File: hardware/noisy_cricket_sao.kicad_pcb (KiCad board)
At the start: 2 copper layers, 30 x 25 mm, 26 parts, among them J1 SAO 6-Pin, U1 AD8107, U2 CH32V003F4U6

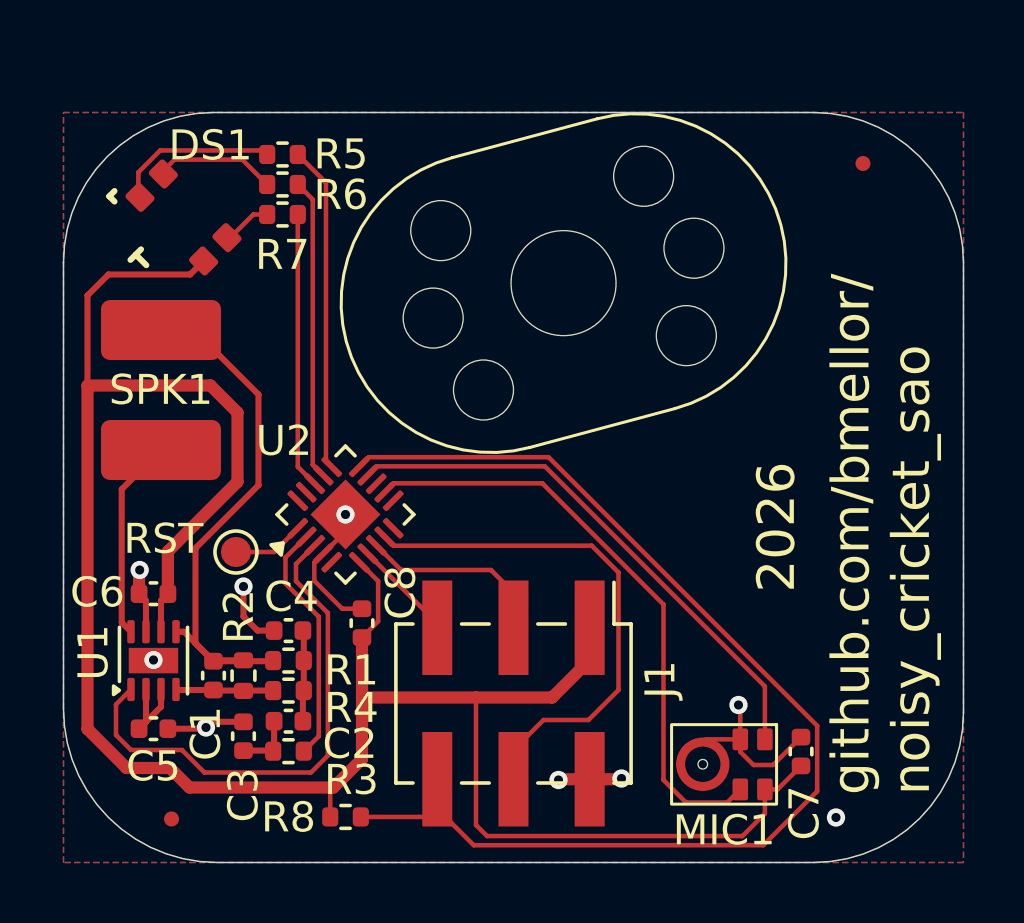
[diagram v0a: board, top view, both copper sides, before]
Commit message: Switch to MSPM0
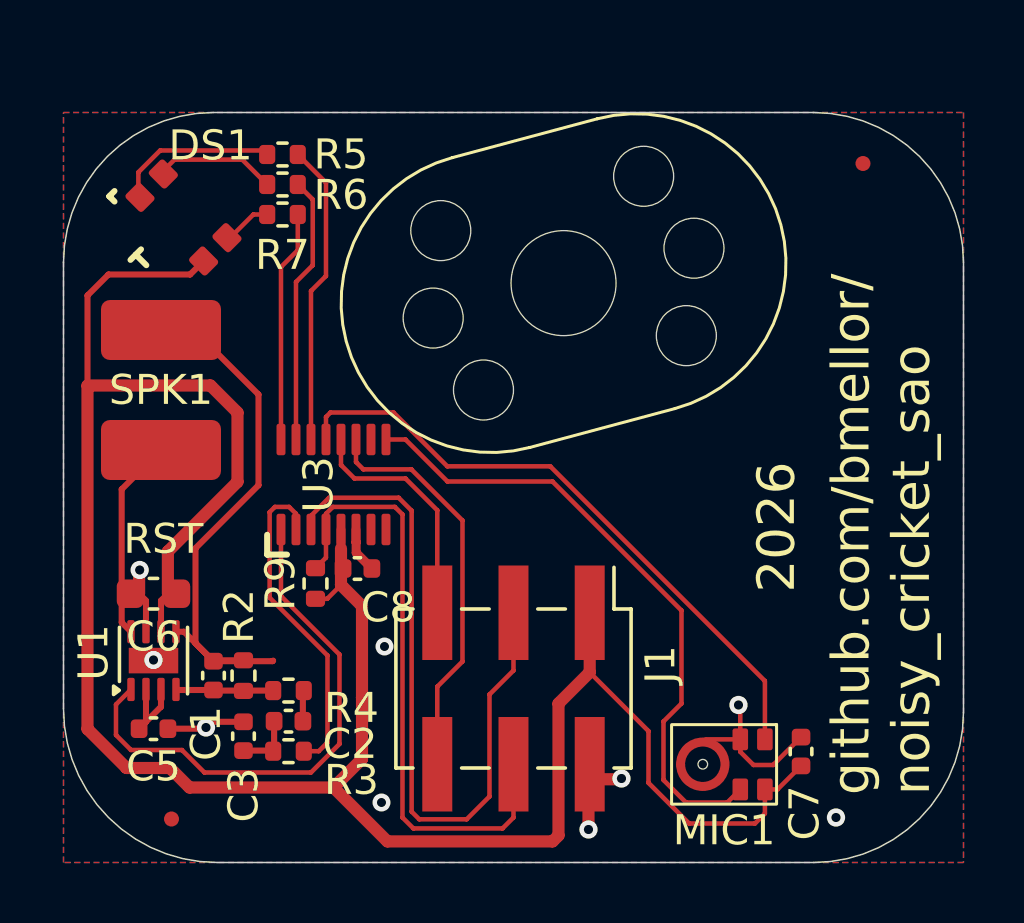
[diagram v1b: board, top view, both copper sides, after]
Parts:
- removed C4: 1.3nF, Capacitor_SMD:C_0402_1005Metric
- removed R1: 26.1k, Resistor_SMD:R_0402_1005Metric
- removed R8: 20k, Resistor_SMD:R_0402_1005Metric
- removed TP1: TestPoint, TestPoint:TestPoint_Pad_D1.0mm
- removed U2: CH32V003F4U6, noisy_cricket_sao:CH32V003F4U6
- added R9: 20k, Resistor_SMD:R_0402_1005Metric, F.Cu at (134.4, 94.7)
- added U3: MSPM0C1104SDYYR, noisy_cricket_sao:SOT23-16-TI, F.Cu at (135.0, 91.4)
- C3: value 390nF -> 22nF
- C6: value 1uF -> 10uF; footprint Capacitor_SMD:C_0402_1005Metric -> Capacitor_SMD:C_0603_1608Metric
- R3: value 40.2 -> 750
- R5: value 100 -> 200
- R6, R7: value 0 -> 100
- moved C8 1.83 mm to (135.8, 94.2), turned to 180 degrees
- moved J1 0.50 mm to (141.0, 98.2)
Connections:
- J1 pad 5: /UART -> /SWCLK
- J1 pad 6: /SWIO -> /SWDIO
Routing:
- net /SWIO: track 37.6 -> 0.00 mm
- net /SDA: track 7.33 -> 24.8 mm
- net /SWDIO: track 0.00 -> 13.5 mm
- net /SWCLK: track 0.00 -> 8.15 mm
- net GND: track 19.1 -> 14.4 mm
- net /UART: track 3.43 -> 0.00 mm
- net /SCL: track 17.5 -> 20.7 mm
- net /PDM_DATA: track 18.2 -> 21.1 mm
- net /AUDIO: track 8.10 -> 11.0 mm
- net +3V3: track 76.8 -> 79.5 mm
- net /RESET: track 2.54 -> 0.00 mm
- net Net-(C2-Pad2): track 3.07 -> 1.06 mm
- net /LED_B: track 9.21 -> 7.73 mm
- net /PDM_CLK: track 20.0 -> 21.2 mm
- net /LED_G: track 10.0 -> 8.94 mm
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
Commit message: Update LPF for 1x gain, tweak footprints and silk
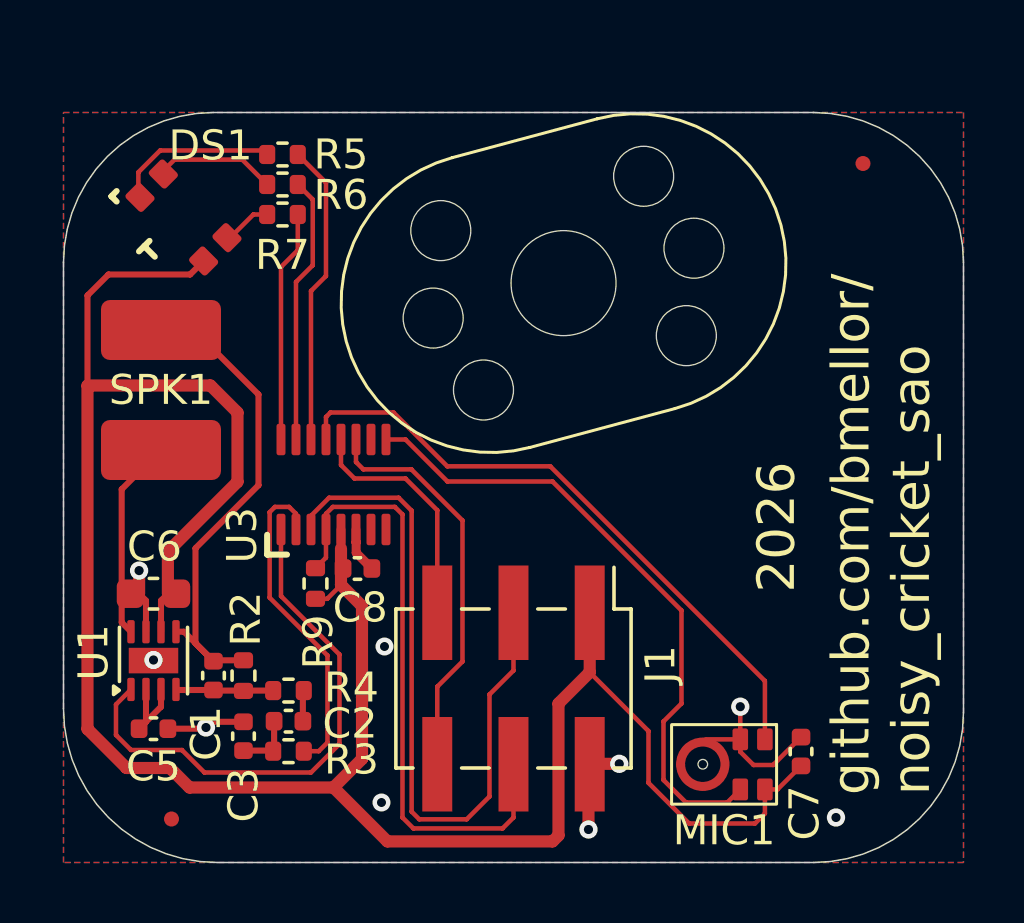
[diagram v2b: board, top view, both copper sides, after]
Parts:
- C1: value 220pF -> 820pF
- C7: value 0.39uF -> 1uF
- R2: value 68k -> 20k
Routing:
- net Net-(SPK1-+): track 18.8 -> 16.8 mm
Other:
- board text removed: "RST"
